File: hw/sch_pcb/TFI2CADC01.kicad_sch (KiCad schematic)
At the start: 19 parts, among them J1 HEADER_2x04, J2 SM04B-GHS-TB, J3 SM04B-GHS-TB, T1 ALERT/RDY, U1 MIC5504-3.3YM5, U2 ADS1115IDGS

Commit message: Improve layout.
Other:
- note added: "0x48 (default)"
- note added: "I2C address selection"
- note removed: "0x48"
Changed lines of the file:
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@@
 		(comment 1 "I2C Analog to digital convertor\\nfor PixHawk ")
 	)
-	(text "0x48\n"
+	(text "0x48 (default)\n"
 		(exclude_from_sim no)
-		(at 115.57 146.558 0)
+		(at 123.19 151.13 0)
+		(effects
+			(font
+				(size 1.27 1.27)
+			)
+			(justify left)
+		)
+	)
+	(text "I2C address selection"
+		(exclude_from_sim no)
+		(at 119.38 142.24 0)
 		(effects
 			(font
@@
 	(text "0x49\n\n"
 		(exclude_from_sim no)
-		(at 125.984 159.004 0)
+		(at 123.19 156.21 0)
 		(effects
 			(font
 				(size 1.27 1.27)
 			)
+			(justify left)
 		)
 	)
@@
 		)
 		(property "Value" "ALERT/RDY"
-			(at 145.034 99.314 0)
+			(at 147.32 96.52 0)
 			(effects
 				(font

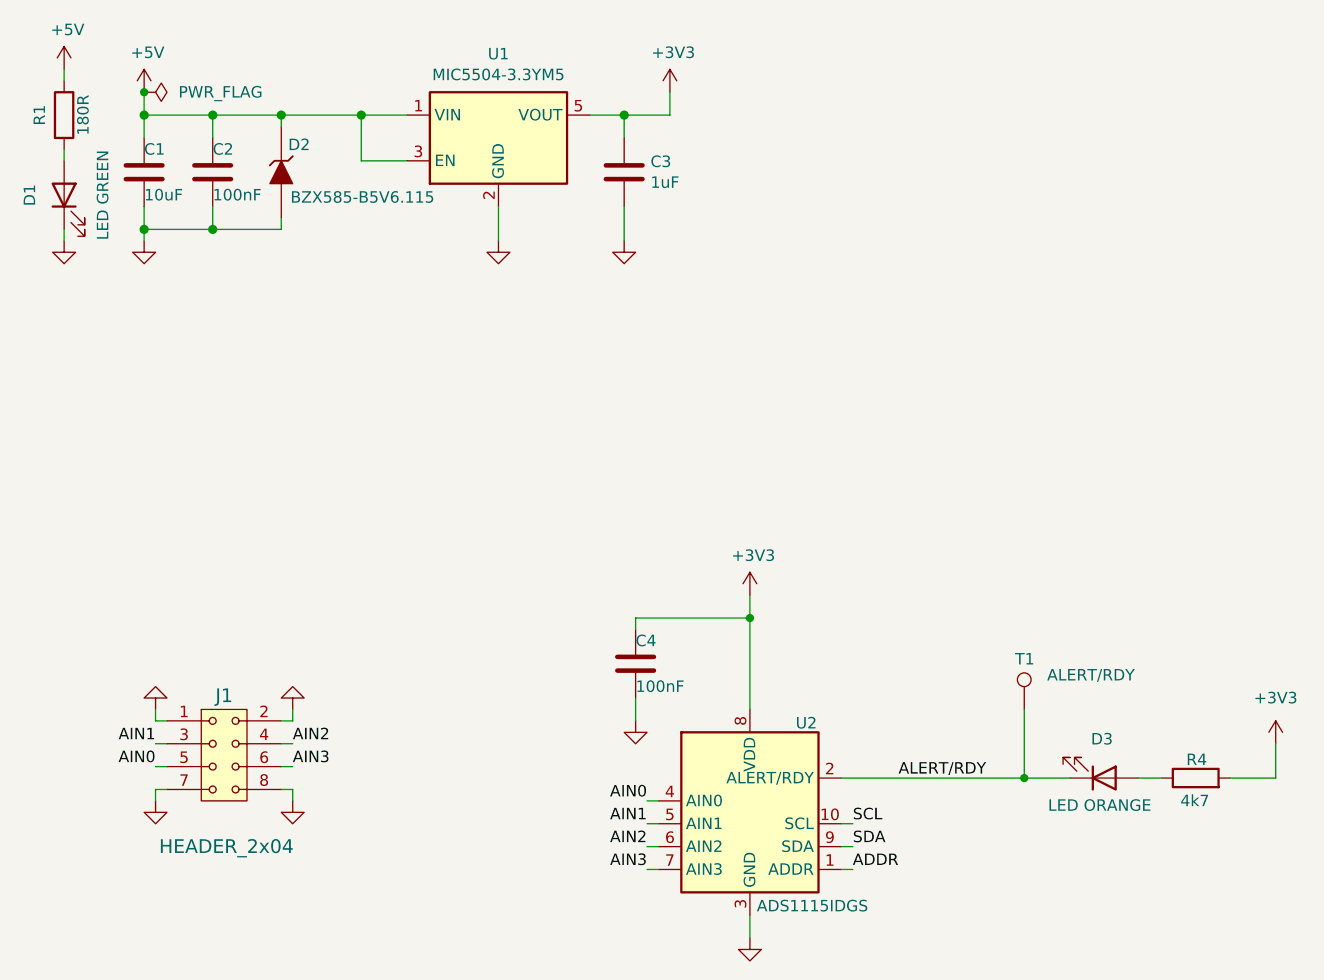
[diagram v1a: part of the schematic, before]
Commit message: Improve layout. Fix DRC and ERC errors. Improve PinHeader edge-mount footprint. Update footprints.
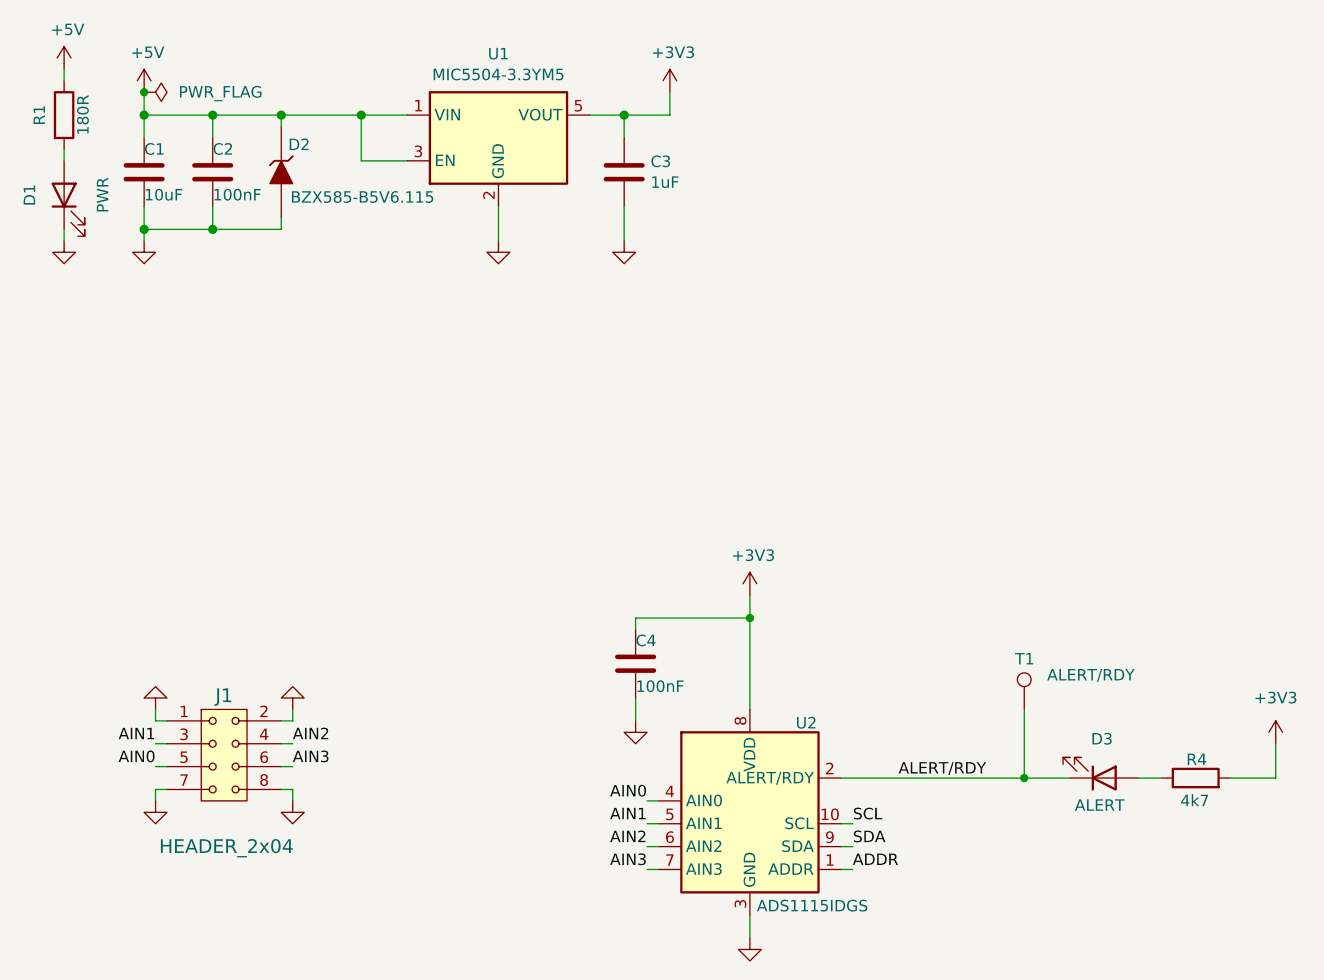
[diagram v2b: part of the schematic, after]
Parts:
- C1: footprint Mlab_R:SMD-0805 -> Capacitor_SMD:C_0805_2012Metric
- C2, C3, C4: footprint Mlab_R:SMD-0603 -> Capacitor_SMD:C_0603_1608Metric
- D1: value LED GREEN -> PWR; footprint Mlab_D:LED_0805 -> LED_SMD:LED_0603_1608Metric
- D3: value LED ORANGE -> ALERT; footprint Mlab_D:LED_0805 -> LED_SMD:LED_0603_1608Metric; UST_ID 60d582331287500165f859d0 -> 60d581db1287500165f859a2
- J1: footprint Connector_PinHeader_2.54mm:PinHeader_2x04_P2.54mm_Edge_Mount -> Mlab_Pin_Headers:PinHeader_2x04_P2.54mm_Edge_Mount
- JP1: footprint Jumper:SolderJumper-3_P1.3mm_Bridged12_Pad1.0x1.5mm_NumberLabels -> Jumper:SolderJumper-3_P1.3mm_Bridged12_RoundedPad1.0x1.5mm
- JP2: footprint Jumper:SolderJumper-2_P1.3mm_Open_Pad1.0x1.5mm -> Jumper:SolderJumper-2_P1.3mm_Open_RoundedPad1.0x1.5mm
- R2, R3, R4: footprint Mlab_R:SMD-0603 -> Resistor_SMD:R_0603_1608Metric
- T1: footprint TestPoint:TestPoint_Keystone_5015_Micro_Mini -> TestPoint:TestPoint_Pad_D2.0mm
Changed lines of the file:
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@@
 			)
 		)
-		(property "Footprint" "Mlab_R:SMD-0603"
+		(property "Footprint" "Capacitor_SMD:C_0603_1608Metric"
 			(at 54.61 40.64 0)
 			(effects
@@
 					(size 1.27 1.27)
 				)
-			)
-		)
-		(property "UST_id" ""
-			(at 54.61 40.64 0)
-			(effects
-				(font
-					(size 1.27 1.27)
-				)
-				(hide yes)
 			)
 		)
@@
 			)
 		)
-		(property "Footprint" "Mlab_R:SMD-0603"
+		(property "Footprint" "Resistor_SMD:R_0603_1608Metric"
 			(at 205.232 92.71 90)
 			(effects
@@
 					(size 1.27 1.27)
 				)
-			)
-		)
-		(property "UST_id" ""
-			(at 207.01 92.71 0)
-			(effects
-				(font
-					(size 1.27 1.27)
-				)
-				(hide yes)
 			)
 		)
@@
 			)
 		)
-		(property "Footprint" "Mlab_R:SMD-0603"
+		(property "Footprint" "Resistor_SMD:R_0603_1608Metric"
 			(at 198.882 92.71 90)
 			(effects
@@
 					(size 1.27 1.27)
 				)
-			)
-		)
-		(property "UST_id" ""
-			(at 200.66 92.71 0)
-			(effects
-				(font
-					(size 1.27 1.27)
-				)
-				(hide yes)
 			)
 		)
@@
 			)
 		)
-		(property "Footprint" "Mlab_R:SMD-0805"
+		(property "Footprint" "Capacitor_SMD:C_0805_2012Metric"
 			(at 46.99 40.64 0)
 			(effects
@@
 					(size 1.27 1.27)
 				)
-			)
-		)
-		(property "UST_id" ""
-			(at 46.99 40.64 0)
-			(effects
-				(font
-					(size 1.27 1.27)
-				)
-				(hide yes)
 			)
 		)
@@
 			)
 		)
-		(property "UST_id" ""
-			(at 62.23 40.64 0)
-			(effects
-				(font
-					(size 1.27 1.27)
-				)
-				(hide yes)
-			)
-		)
 		(property "UST_ID" "60879d38128750769ee58e48"
 			(at 62.23 40.64 0)
@@
 			)
 		)
-		(property "UST_id" ""
-			(at 86.36 36.83 0)
-			(effects
-				(font
-					(size 1.27 1.27)
-				)
-				(hide yes)
-			)
-		)
 		(property "UST_ID" "5c7255e81287500b4e112ea2"
 			(at 86.36 36.83 0)
@@
 			)
 		)
-		(property "UST_id" ""
-			(at 222.25 102.87 0)
-			(effects
-				(font
-					(size 1.27 1.27)
-				)
-				(hide yes)
-			)
-		)
 		(property "UST_ID" "5c86273d1287500b4e0280be"
 			(at 222.25 102.87 0)
@@
 			)
 		)
-		(property "Footprint" "Mlab_R:SMD-0603"
+		(property "Footprint" "Capacitor_SMD:C_0603_1608Metric"
 			(at 101.2952 44.45 0)
 			(effects
@@
 					(size 1.27 1.27)
 				)
-			)
-		)
-		(property "UST_id" ""
-			(at 100.33 40.64 0)
-			(effects
-				(font
-					(size 1.27 1.27)
-				)
-				(hide yes)
 			)
 		)
@@
 	)
 	(symbol
-		(lib_name "+3V3_1")
 		(lib_id "power:+3V3")
 		(at 172.72 104.14 0)
@@
 			)
 		)
-		(property "Footprint" "Jumper:SolderJumper-3_P1.3mm_Bridged12_Pad1.0x1.5mm_NumberLabels"
+		(property "Footprint" "Jumper:SolderJumper-3_P1.3mm_Bridged12_RoundedPad1.0x1.5mm"
 			(at 118.11 152.4 0)
 			(effects
@@
 			)
 		)
+		(property "UST_ID" ""
+			(at 118.11 152.4 0)
+			(effects
+				(font
+					(size 1.27 1.27)
+				)
+				(hide yes)
+			)
+		)
 		(pin "1"
 		)
@@
 			)
 		)
-		(property "Footprint" "Jumper:SolderJumper-2_P1.3mm_Open_Pad1.0x1.5mm"
+		(property "Footprint" "Jumper:SolderJumper-2_P1.3mm_Open_RoundedPad1.0x1.5mm"
 			(at 119.38 163.83 0)
 			(effects
@@
 		)
 		(property "Description" "Solder Jumper, 2-pole, open"
+			(at 119.38 163.83 0)
+			(effects
+				(font
+					(size 1.27 1.27)
+				)
+				(hide yes)
+			)
+		)
+		(property "UST_ID" ""
 			(at 119.38 163.83 0)
 			(effects
@@
 			)
 		)
-		(property "Value" "LED ORANGE"
+		(property "Value" "ALERT"
 			(at 153.162 110.998 0)
 			(effects
@@
 			)
 		)
-		(property "Footprint" "Mlab_D:LED_0805"
+		(property "Footprint" "LED_SMD:LED_0603_1608Metric"
 			(at 153.67 107.95 0)
 			(effects
@@
 			)
 		)
-		(property "UST_id" ""
-			(at 153.67 107.95 0)
-			(effects
-				(font
-					(size 1.27 1.27)
-				)
-				(hide yes)
-			)
-		)
-		(property "UST_ID" "60d582331287500165f859d0"
+		(property "UST_ID" "60d581db1287500165f859a2"
 			(at 153.67 107.95 0)
 			(effects
@@
 			)
 		)
-		(property "Value" "LED GREEN"
+		(property "Value" "PWR"
 			(at 42.418 43.18 0)
 			(effects
@@
 			)
 		)
-		(property "Footprint" "Mlab_D:LED_0805"
+		(property "Footprint" "LED_SMD:LED_0603_1608Metric"
 			(at 38.1 43.18 0)
 			(effects
@@
 					(size 1.27 1.27)
 				)
-			)
-		)
-		(property "UST_id" ""
-			(at 38.1 43.18 0)
-			(effects
-				(font
-					(size 1.27 1.27)
-				)
-				(hide yes)
 			)
 		)
@@
 			)
 		)
-		(property "Footprint" "Connector_PinHeader_2.54mm:PinHeader_2x04_P2.54mm_Edge_Mount"
+		(property "Footprint" "Mlab_Pin_Headers:PinHeader_2x04_P2.54mm_Edge_Mount"
 			(at 55.88 101.6 0)
 			(effects
@@
 			)
 		)
+		(property "UST_ID" ""
+			(at 55.88 105.41 0)
+			(effects
+				(font
+					(size 1.27 1.27)
+				)
+				(hide yes)
+			)
+		)
 		(pin "7"
 		)
@@
 			)
 		)
-		(property "Footprint" "Mlab_R:SMD-0603"
+		(property "Footprint" "Capacitor_SMD:C_0603_1608Metric"
 			(at 101.6 95.25 0)
 			(effects
@@
 					(size 1.27 1.27)
 				)
-			)
-		)
-		(property "UST_id" ""
-			(at 101.6 95.25 0)
-			(effects
-				(font
-					(size 1.27 1.27)
-				)
-				(hide yes)
 			)
 		)
@@
 			)
 		)
-		(property "Footprint" "TestPoint:TestPoint_Keystone_5015_Micro_Mini"
+		(property "Footprint" "TestPoint:TestPoint_Pad_D2.0mm"
 			(at 149.86 100.33 0)
 			(effects
@@
 			)
 		)
+		(property "UST_ID" ""
+			(at 144.78 100.33 0)
+			(effects
+				(font
+					(size 1.27 1.27)
+				)
+				(hide yes)
+			)
+		)
 		(pin "1"
 		)
@@
 	)
 	(symbol
-		(lib_name "GND_1")
 		(lib_id "power:GND")
 		(at 38.1 48.26 0)
@@
 			)
 		)
-		(property "UST_id" ""
-			(at 261.62 102.87 0)
-			(effects
-				(font
-					(size 1.27 1.27)
-				)
-				(hide yes)
-			)
-		)
 		(property "UST_ID" "5c86273d1287500b4e0280be"
 			(at 261.62 102.87 0)
@@
 					(size 1.27 1.27)
 				)
-			)
-		)
-		(property "UST_id" ""
-			(at 38.1 34.29 0)
-			(effects
-				(font
-					(size 1.27 1.27)
-				)
-				(hide yes)
 			)
 		)
@@
 			)
 		)
-		(property "Footprint" "Mlab_R:SMD-0603"
+		(property "Footprint" "Resistor_SMD:R_0603_1608Metric"
 			(at 163.83 109.728 90)
 			(effects
@@
 			)
 		)
-		(property "UST_id" ""
-			(at 163.83 107.95 0)
-			(effects
-				(font
-					(size 1.27 1.27)
-				)
-				(hide yes)
-			)
-		)

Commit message: Improve footprint selection. Fix layout Documentation update.
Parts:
- U2: footprint Package_SO:TSSOP-10_3x3mm_P0.5mm -> Package_SO:VSSOP-10_3x3mm_P0.5mm; UST_ID (none) -> 6934a81dea235ce78ba25ac5
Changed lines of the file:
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@@
 			)
 		)
-		(property "Footprint" "Package_SO:TSSOP-10_3x3mm_P0.5mm"
+		(property "Footprint" "Package_SO:VSSOP-10_3x3mm_P0.5mm"
 			(at 114.3 125.73 0)
 			(effects
@@
 			(at 114.3 113.03 0)
 			(effects
+				(font
+					(size 1.27 1.27)
+				)
+				(hide yes)
+			)
+		)
+		(property "UST_ID" "6934a81dea235ce78ba25ac5"
+			(at 114.3 113.03 0)
+			(effects
